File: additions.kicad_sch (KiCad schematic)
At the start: 21 parts, among them J5 SR5-3V-200-1C, J6 SR5-3V-200-1C, J8_SW2 Conn_01x02_Pin, J8_SW3 Conn_01x02_Pin, K2 SR11-3V-200-2C, Q1 CNY74-2H, Q2 CNY74-2H

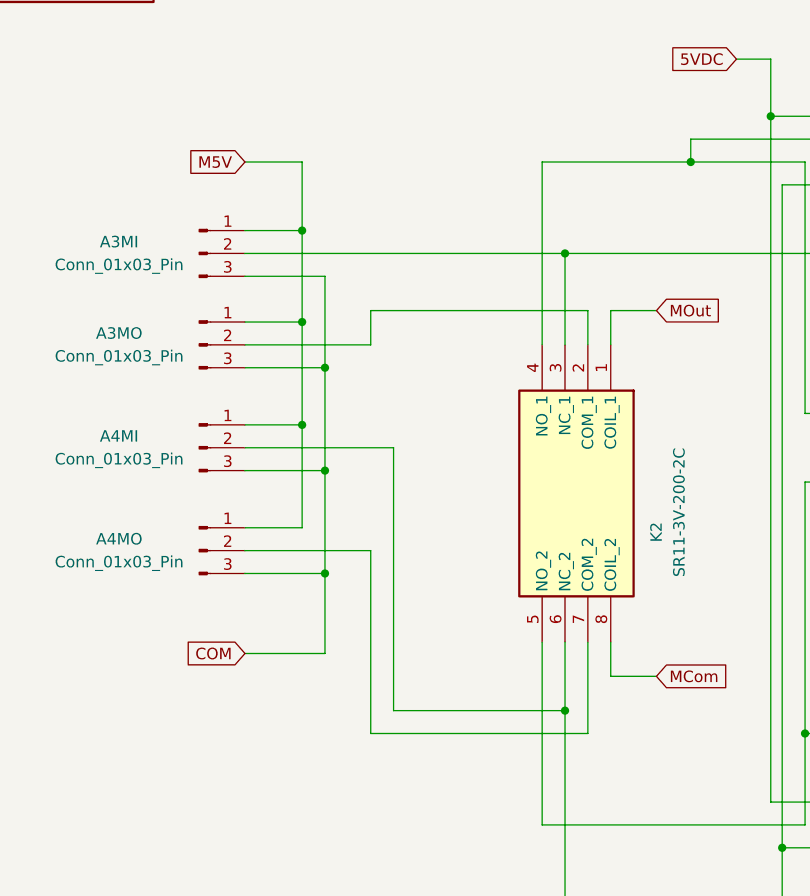
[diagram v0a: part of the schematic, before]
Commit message: Swapped Signal and 5+
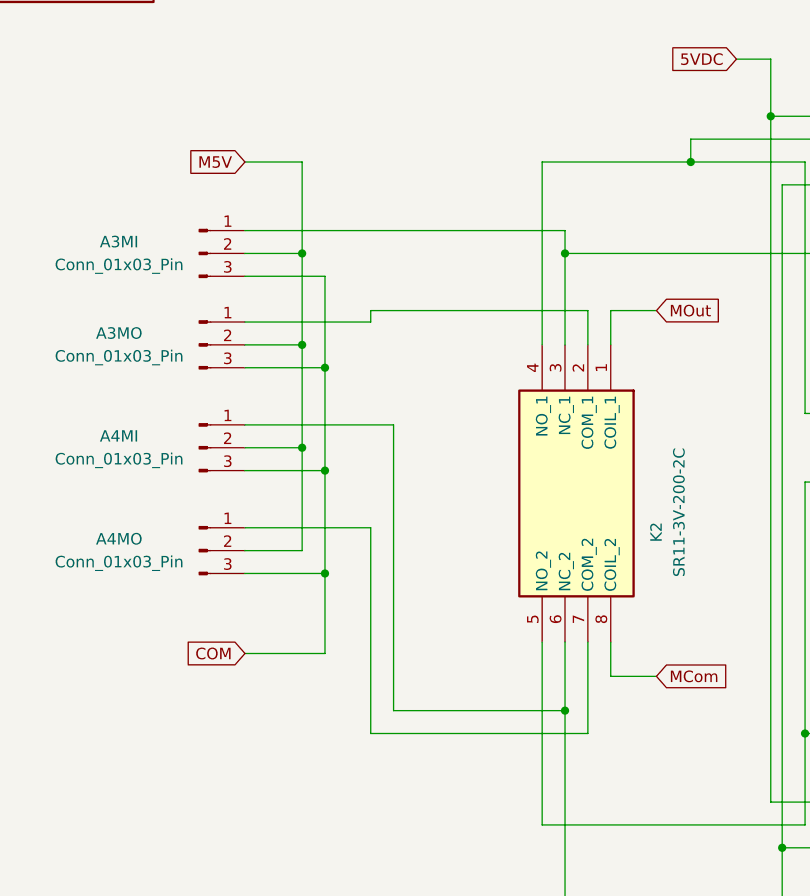
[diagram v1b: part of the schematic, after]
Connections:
- net M5V: now also A3MI.2 (Pin_2), A3MO.2 (Pin_2), A4MI.2 (Pin_2), A4MO.2 (Pin_2); no longer A3MI.1 (Pin_1), A3MO.1 (Pin_1), A4MI.1 (Pin_1), A4MO.1 (Pin_1)
- net at K2.6 (NC_2), R17.1: now also A4MI.1 (Pin_1); no longer A4MI.2 (Pin_2)
- net at K2.2 (COM_1): now also A3MO.1 (Pin_1); no longer A3MO.2 (Pin_2)
- net at K2.7 (COM_2): now also A4MO.1 (Pin_1); no longer A4MO.2 (Pin_2)
- net at K2.3 (NC_1), R17.1: now also A3MI.1 (Pin_1); no longer A3MI.2 (Pin_2)
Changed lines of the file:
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@@
     (title "Additional Circuits")
     (rev "1.1")
-    (comment 1 "AC3 and AC4 Wires Swapped")
+    (comment 1 "Swapped Signal and 5+")
   )
   (junction (at 115.57 36.83) (diameter 0) (color 0 0 0 0)
@@
   (junction (at 181.61 86.36) (diameter 0) (color 0 0 0 0)
   )
-  (junction (at 121.92 100.33) (diameter 0) (color 0 0 0 0)
-  )
   (junction (at 151.13 132.08) (diameter 0) (color 0 0 0 0)
   )
   (junction (at 177.8 134.62) (diameter 0) (color 0 0 0 0)
   )
+  (junction (at 121.92 91.44) (diameter 0) (color 0 0 0 0)
+  )
   (junction (at 201.93 96.52) (diameter 0) (color 0 0 0 0)
   )
   (junction (at 217.17 72.39) (diameter 0) (color 0 0 0 0)
   )
+  (junction (at 121.92 102.87) (diameter 0) (color 0 0 0 0)
+  )
   (junction (at 165.1 71.12) (diameter 0) (color 0 0 0 0)
   )
-  (junction (at 121.92 78.74) (diameter 0) (color 0 0 0 0)
-  )
   (junction (at 181.61 123.19) (diameter 0) (color 0 0 0 0)
   )
@@
   (junction (at 124.46 105.41) (diameter 0) (color 0 0 0 0)
   )
-  (junction (at 121.92 88.9) (diameter 0) (color 0 0 0 0)
+  (junction (at 151.13 81.28) (diameter 0) (color 0 0 0 0)
   )
   (junction (at 124.46 116.84) (diameter 0) (color 0 0 0 0)
   )
-  (junction (at 151.13 81.28) (diameter 0) (color 0 0 0 0)
-  )
-  (wire (pts (xy 132.08 102.87) (xy 132.08 132.08))
+  (junction (at 121.92 81.28) (diameter 0) (color 0 0 0 0)
+  )
+  (wire (pts (xy 132.08 100.33) (xy 132.08 132.08))
     (stroke (width 0) (type default))
   )
@@
     (stroke (width 0) (type default))
   )
-  (wire (pts (xy 115.57 100.33) (xy 121.92 100.33))
-    (stroke (width 0) (type default))
-  )
-  (wire (pts (xy 121.92 111.76) (xy 115.57 111.76))
-    (stroke (width 0) (type default))
-  )
   (wire (pts (xy 185.42 134.62) (xy 177.8 134.62))
     (stroke (width 0) (type default))
@@
     (stroke (width 0) (type default))
   )
+  (wire (pts (xy 115.57 102.87) (xy 121.92 102.87))
+    (stroke (width 0) (type default))
+  )
   (wire (pts (xy 165.1 68.58) (xy 185.42 68.58))
     (stroke (width 0) (type default))
@@
     (stroke (width 0) (type default))
   )
-  (wire (pts (xy 115.57 78.74) (xy 121.92 78.74))
-    (stroke (width 0) (type default))
-  )
   (wire (pts (xy 186.69 95.25) (xy 181.61 95.25))
     (stroke (width 0) (type default))
@@
     (stroke (width 0) (type default))
   )
+  (wire (pts (xy 121.92 102.87) (xy 121.92 114.3))
+    (stroke (width 0) (type default))
+  )
   (wire (pts (xy 175.26 147.32) (xy 185.42 147.32))
     (stroke (width 0) (type default))
@@
     (stroke (width 0) (type default))
   )
-  (wire (pts (xy 121.92 71.12) (xy 121.92 78.74))
-    (stroke (width 0) (type default))
-  )
   (wire (pts (xy 115.57 25.4) (xy 115.57 36.83))
     (stroke (width 0) (type default))
   )
-  (wire (pts (xy 129.54 114.3) (xy 115.57 114.3))
-    (stroke (width 0) (type default))
-  )
   (wire (pts (xy 205.74 107.95) (xy 201.93 107.95))
     (stroke (width 0) (type default))
@@
     (stroke (width 0) (type default))
   )
-  (wire (pts (xy 129.54 87.63) (xy 129.54 91.44))
+  (wire (pts (xy 115.57 91.44) (xy 121.92 91.44))
     (stroke (width 0) (type default))
   )
@@
     (stroke (width 0) (type default))
   )
-  (wire (pts (xy 129.54 134.62) (xy 129.54 114.3))
-    (stroke (width 0) (type default))
-  )
-  (wire (pts (xy 115.57 102.87) (xy 132.08 102.87))
+  (wire (pts (xy 129.54 111.76) (xy 129.54 134.62))
     (stroke (width 0) (type default))
   )
@@
     (stroke (width 0) (type default))
   )
+  (wire (pts (xy 121.92 81.28) (xy 121.92 91.44))
+    (stroke (width 0) (type default))
+  )
   (wire (pts (xy 151.13 162.56) (xy 151.13 132.08))
     (stroke (width 0) (type default))
@@
     (stroke (width 0) (type default))
   )
-  (wire (pts (xy 115.57 88.9) (xy 121.92 88.9))
-    (stroke (width 0) (type default))
-  )
   (wire (pts (xy 201.93 95.25) (xy 201.93 96.52))
     (stroke (width 0) (type default))
@@
     (stroke (width 0) (type default))
   )
+  (wire (pts (xy 151.13 78.74) (xy 151.13 81.28))
+    (stroke (width 0) (type default))
+  )
   (wire (pts (xy 194.31 110.49) (xy 181.61 110.49))
     (stroke (width 0) (type default))
   )
+  (wire (pts (xy 115.57 81.28) (xy 121.92 81.28))
+    (stroke (width 0) (type default))
+  )
   (wire (pts (xy 185.42 73.66) (xy 175.26 73.66))
     (stroke (width 0) (type default))
@@
     (stroke (width 0) (type default))
   )
+  (wire (pts (xy 121.92 71.12) (xy 121.92 81.28))
+    (stroke (width 0) (type default))
+  )
+  (wire (pts (xy 129.54 88.9) (xy 129.54 87.63))
+    (stroke (width 0) (type default))
+  )
   (wire (pts (xy 48.26 24.13) (xy 48.26 25.4))
     (stroke (width 0) (type default))
@@
     (stroke (width 0) (type default))
   )
-  (wire (pts (xy 121.92 100.33) (xy 121.92 111.76))
-    (stroke (width 0) (type default))
-  )
   (wire (pts (xy 50.8 22.86) (xy 50.8 24.13))
     (stroke (width 0) (type default))
@@
     (stroke (width 0) (type default))
   )
-  (wire (pts (xy 129.54 91.44) (xy 115.57 91.44))
-    (stroke (width 0) (type default))
-  )
   (wire (pts (xy 201.93 99.06) (xy 201.93 96.52))
     (stroke (width 0) (type default))
@@
     (stroke (width 0) (type default))
   )
-  (wire (pts (xy 115.57 81.28) (xy 151.13 81.28))
-    (stroke (width 0) (type default))
-  )
   (wire (pts (xy 215.9 144.78) (xy 215.9 146.05))
     (stroke (width 0) (type default))
   )
+  (wire (pts (xy 121.92 114.3) (xy 115.57 114.3))
+    (stroke (width 0) (type default))
+  )
   (wire (pts (xy 210.82 144.78) (xy 215.9 144.78))
     (stroke (width 0) (type default))
@@
     (stroke (width 0) (type default))
   )
-  (wire (pts (xy 121.92 78.74) (xy 121.92 88.9))
-    (stroke (width 0) (type default))
-  )
   (wire (pts (xy 173.99 59.69) (xy 173.99 66.04))
     (stroke (width 0) (type default))
@@
     (stroke (width 0) (type default))
   )
+  (wire (pts (xy 115.57 78.74) (xy 151.13 78.74))
+    (stroke (width 0) (type default))
+  )
   (wire (pts (xy 115.57 125.73) (xy 124.46 125.73))
     (stroke (width 0) (type default))
@@
     (stroke (width 0) (type default))
   )
+  (wire (pts (xy 115.57 111.76) (xy 129.54 111.76))
+    (stroke (width 0) (type default))
+  )
   (wire (pts (xy 231.14 162.56) (xy 151.13 162.56))
     (stroke (width 0) (type default))
@@
     (stroke (width 0) (type default))
   )
+  (wire (pts (xy 121.92 91.44) (xy 121.92 102.87))
+    (stroke (width 0) (type default))
+  )
   (wire (pts (xy 185.42 71.12) (xy 179.07 71.12))
     (stroke (width 0) (type default))
@@
     (stroke (width 0) (type default))
   )
+  (wire (pts (xy 115.57 100.33) (xy 132.08 100.33))
+    (stroke (width 0) (type default))
+  )
   (wire (pts (xy 215.9 146.05) (xy 223.52 146.05))
     (stroke (width 0) (type default))
@@
     (stroke (width 0) (type default))
   )
-  (wire (pts (xy 121.92 88.9) (xy 121.92 100.33))
-    (stroke (width 0) (type default))
-  )
   (wire (pts (xy 66.04 48.26) (xy 77.47 48.26))
     (stroke (width 0) (type default))
   )
+  (wire (pts (xy 115.57 88.9) (xy 129.54 88.9))
+    (stroke (width 0) (type default))
+  )
